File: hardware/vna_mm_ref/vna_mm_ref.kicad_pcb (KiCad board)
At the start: 4 copper layers, 213 parts, among them J201 Conn_Coaxial, J202 Conn_Coaxial, J401 Conn_Coaxial, J402 Conn_Coaxial, J501 Conn_02x10_Counter_Clockwise, K401 1-1462051-1, Q501 FDS6890A, SW501 SW_DIP_x02, SW502 SW_DIP_x02, U201 LTC6957xDD-3, U301 HMC1031, U401 DOCAT050F-010.0M, U402 74AHC1G04, U403 DRV8837C, U404 LTC6957xDD-3, U501 LTC4365DDB, U502 ADP7156, U503 ADP7156, U504 74AHC244, U505 LMT84DCK, X301 ABLNO-V-100.000MHZ

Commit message: layout of 100 MHz reference board
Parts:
- added H509: M.2, MountingHole:MountingHole_2.2mm_M2_Pad_Via, F.Cu at (161.2, 68.0)
- added H510: M.2, MountingHole:MountingHole_2.2mm_M2_Pad_Via, F.Cu at (158.2, 102.0)
- added H512: M.2, MountingHole:MountingHole_2.2mm_M2_Pad_Via, F.Cu at (208.0, 67.5)
- added H513: M.2, MountingHole:MountingHole_2.2mm_M2_Pad_Via, F.Cu at (251.5, 42.0)
- added H514: M.2, MountingHole:MountingHole_2.2mm_M2_Pad_Via, F.Cu at (196.0, 102.0)
- added H515: M.2, MountingHole:MountingHole_2.2mm_M2_Pad_Via, F.Cu at (141.5, 42.0)
- added H516: M.2, MountingHole:MountingHole_2.2mm_M2_Pad_Via, F.Cu at (186.0, 68.0)
- added J502: Conn_01x07, Connector_PinHeader_2.54mm:PinHeader_1x07_P2.54mm_Vertical, F.Cu at (188.0, 45.7)
- added R537: 10k, Resistor_SMD:R_0402_1005Metric, F.Cu at (213.8, 61.5)
- added TP504: TestPoint, vna_mm:TURRET_MILLMAX_2101, F.Cu at (141.5, 50.5)
- J501: value Conn_02x10_Counter_Clockwise -> Conn_02x10_Odd_Even; footprint Connector_PinHeader_2.54mm:PinHeader_2x11_P2.54mm_Vertical -> Connector_PinHeader_2.54mm:PinHeader_2x10_P2.54mm_Vertical
- TP503: value FAULT -> TestPoint; footprint TestPoint:TestPoint_Keystone_5015_Micro-Minature -> vna_mm:TURRET_MILLMAX_2101
- moved R515 246.7 mm to (250.5, 59.5)
- moved SW501 236.6 mm to (245.0, 58.5), turned to 180 degrees
- moved R520 227.1 mm to (239.5, 56.0), turned to 270 degrees
- moved R524 224.1 mm to (239.5, 59.0), turned to 270 degrees
- moved J501 192.1 mm to (210.8, 40.6), turned to 270 degrees
- moved R516 177.0 mm to (179.5, 57.5)
- moved C525 176.8 mm to (231.5, 60.2), turned to 0 degrees
- moved SW502 176.2 mm to (186.0, 59.0)
- moved R527 176.2 mm to (229.0, 59.2)
- moved C523 175.3 mm to (234.5, 59.7), turned to 270 degrees
- moved U505 173.3 mm to (232.0, 58.2)
- moved R521 172.3 mm to (185.5, 54.0)
- moved R525 172.3 mm to (188.0, 54.0)
- moved R509 167.8 mm to (217.5, 47.5), turned to 270 degrees
- moved D501 165.4 mm to (217.5, 50.7), turned to 270 degrees
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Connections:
- C527 pad 1: /PLL_EN -> /power_conn/INT_REF_EN
- J501 pad 10: GND -> /power_conn/SD_PLLCLK_EXT
- J501 pad 11: /power_conn/REF_SEL_EXT -> GND
- J501 pad 12: /power_conn/INT_REF_EN_EXT -> /power_conn/SD_REFOUT_EXT
- J501 pad 13: /power_conn/SD2_OUTPUT_EXT -> GND
- J501 pad 15: /power_conn/SD_REFOUT_EXT -> GND
- J501 pad 16: /power_conn/SD_PLLCLK_EXT -> /power_conn/SD2_OUTPUT_EXT
- J501 pad 17: /power_conn/RELAY_EN_EXT -> /power_conn/TEMP_SENSE
- J501 pad 18: (no net) -> /power_conn/INT_REF_EN_EXT
- J501 pad 2: VPP -> GND
- J501 pad 20: GND -> /power_conn/REF_SEL_EXT
- J501 pad 4: VPP -> GND
- J501 pad 6: GND -> /power_conn/LKD_EXT
- J501 pad 8: GND -> /power_conn/RELAY_EN_EXT
- J501 pad 9: /power_conn/TEMP_SENSE -> GND
- R302 pad 1: /PLL_EN -> +3V3
- R303 pad 2: /PLL_EN -> +3V3
- R501 pad 2: (no net) -> /power_conn/INT_REF_EN
- R534 pad 1: /PLL_EN -> /power_conn/INT_REF_EN
- TP503 pad 1: Net-(D504-Pad1) -> GND
- U201 pad 10: Net-(R206-Pad1) -> Net-(R207-Pad1)
- U201 pad 9: Net-(R207-Pad1) -> Net-(R206-Pad1)
- U504 pad 15: /power_conn/SD_REFOUT_EXT -> /power_conn/INT_REF_EN_EXT
- U504 pad 17: /power_conn/SD_PLLCLK_EXT -> /power_conn/REF_SEL_EXT
- U504 pad 6: /power_conn/REF_SEL_EXT -> /power_conn/SD_PLLCLK_EXT
- U504 pad 8: /power_conn/INT_REF_EN_EXT -> /power_conn/SD_REFOUT_EXT
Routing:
- net GND: track 0.00 -> 83.1 mm, vias 0 -> 107
- net Net-(C309-Pad1): track 0.00 -> 24.3 mm
- net Net-(K401-Pad11): track 0.00 -> 22.1 mm
- net Net-(C424-Pad2): track 0.00 -> 15.5 mm
- net Net-(K401-Pad1): track 0.00 -> 14.7 mm
- net +4V: track 0.00 -> 12.3 mm
- net Net-(C307-Pad2): track 0.00 -> 11.4 mm
- net Net-(C303-Pad1): track 0.00 -> 10.5 mm
- net Net-(C410-Pad1): track 0.00 -> 10.3 mm
- net Net-(C401-Pad2): track 0.00 -> 9.29 mm
- net Net-(C402-Pad2): track 0.00 -> 8.94 mm
- net Net-(C213-Pad2): track 0.00 -> 8.55 mm
- net Net-(K401-Pad14): track 0.00 -> 8.28 mm
- net Net-(C207-Pad1): track 0.00 -> 8.11 mm
- net Net-(C306-Pad1): track 0.00 -> 8.08 mm
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- added copper zone on F.Cu, net GND
- added copper zone on In1.Cu, net GND
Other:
- board outline added: 115.5 x 66 mm
- net class Default: clearance 0.2 -> 0.15; via_dia 0.8 -> 0.55; via_drill 0.4 -> 0.3
- rule trace_clearance: 0.2 -> 0.15
- rule trace_min: 0.2 -> 0.14
- rule via_min_drill: 0.3 -> 0.2
- rule via_min_size: 0.4 -> 0.45
- board text added: "4V"
- board text added: "EXT_CLK"
- board text added: "GND"
- board text added: "LKD"
- board text added: "REFOUT"
- board text added: "REF_EN"
- board text added: "REF_SEL"
- board text added: "RLY_EN"
- board text added: "SD1_OUT"
- board text added: "SD2_OUT"
- board text added: "TODO: VERIFY RELAY FOOTPRINT"
- board text added: "low phase noise 100 MHz reference 2019.11"

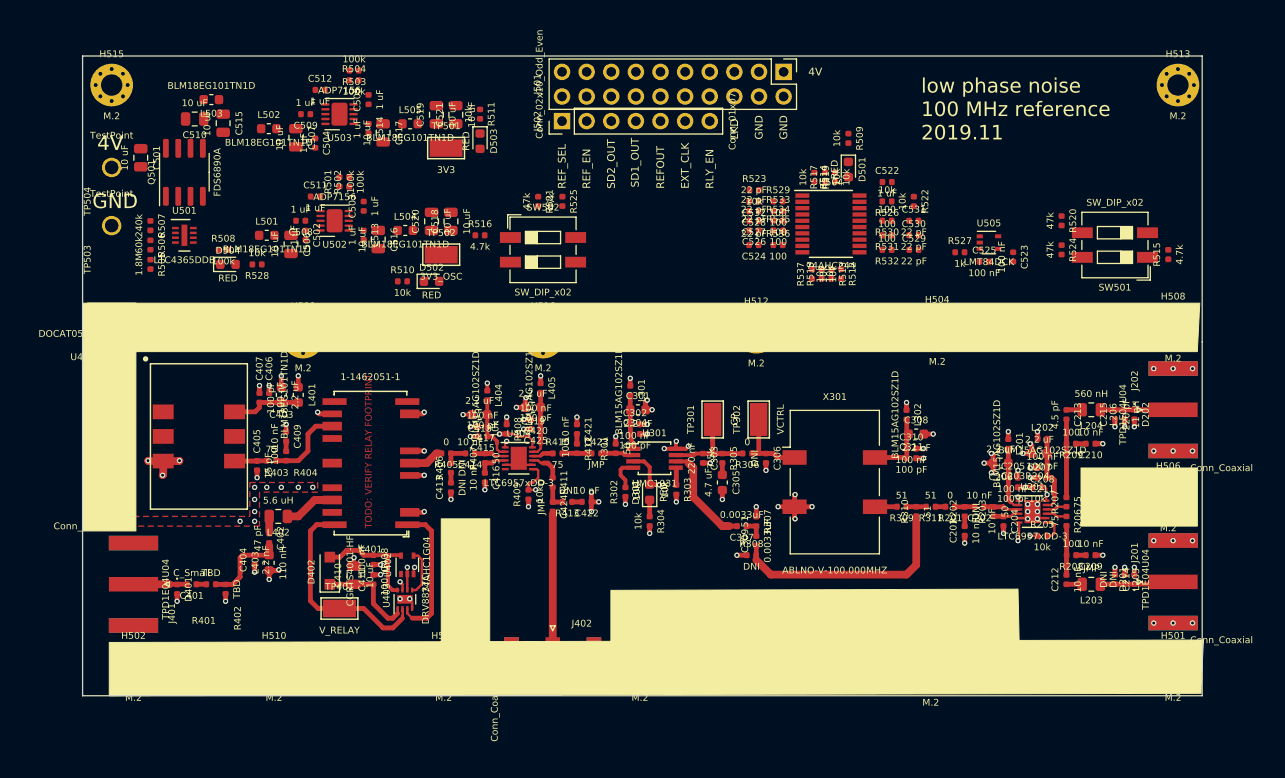
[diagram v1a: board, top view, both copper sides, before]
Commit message: work on layout of vna mm ref board
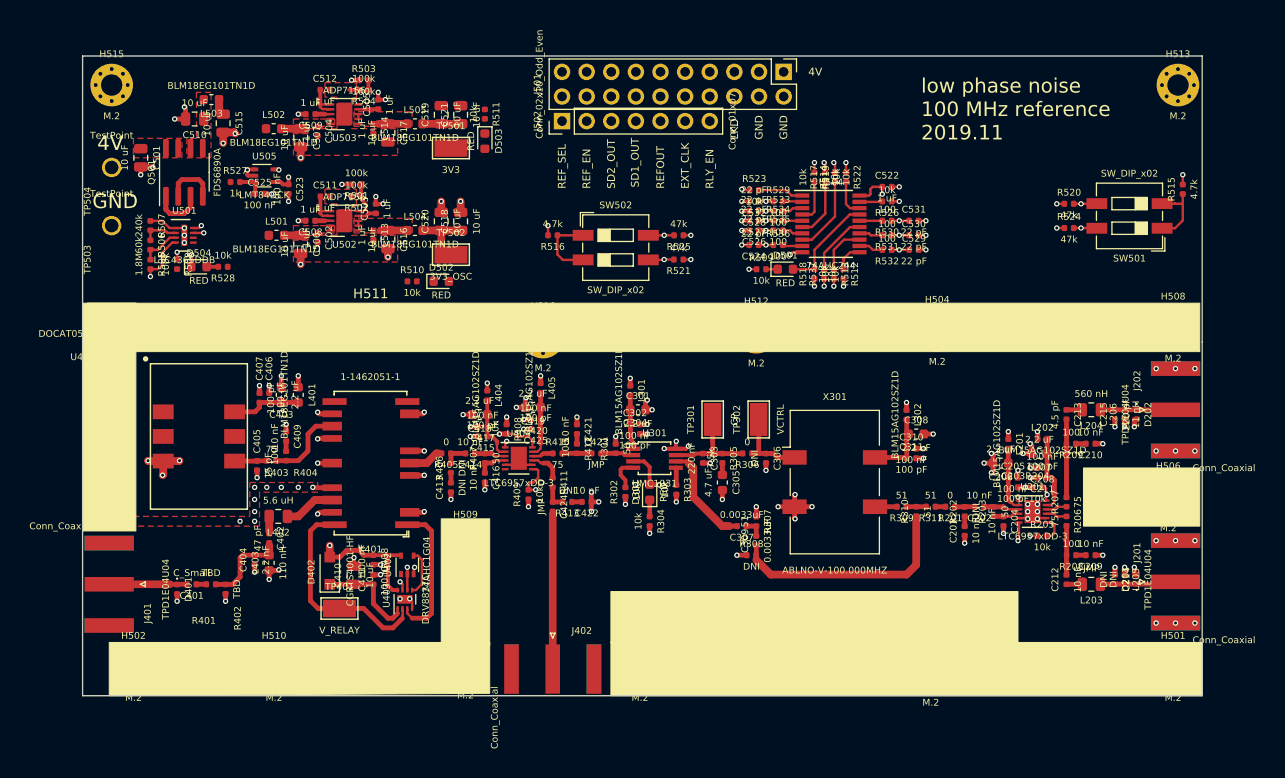
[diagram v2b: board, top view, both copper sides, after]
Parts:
- added H511: M.2, MountingHole:MountingHole_2.2mm_M2_Pad_Via, F.Cu at (168.2, 66.7)
- moved R527 75.1 mm to (154.2, 52.0)
- moved C523 75.1 mm to (159.8, 52.7)
- moved C525 75.1 mm to (156.8, 53.2)
- moved U505 75.1 mm to (157.2, 51.4)
- moved H509 27.3 mm to (178.0, 89.5)
- moved R509 16.2 mm to (208.5, 61.0), turned to 0 degrees
- moved R521 15.7 mm to (200.0, 60.0), turned to 180 degrees
- moved R525 12.5 mm to (200.0, 57.5), turned to 180 degrees
- moved D501 12.2 mm to (211.0, 61.0), turned to 0 degrees
- moved SW502 7.50 mm to (193.5, 58.8)
- moved R516 7.50 mm to (187.0, 57.5), turned to 180 degrees
- moved R522 7.43 mm to (217.2, 51.5)
- moved R515 6.90 mm to (252.0, 52.8)
- moved R508 5.00 mm to (148.2, 60.5), turned to 270 degrees
- moved R528 3.52 mm to (153.0, 60.8)
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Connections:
- K401 pad 15: (no net) -> GND
- K401 pad 17: (no net) -> GND
- K401 pad 19: (no net) -> GND
- K401 pad 21: (no net) -> GND
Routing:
- net GND: track 83.1 -> 133.8 mm, vias 107 -> 155
- net +3V3: track 6.19 -> 19.6 mm, vias 8 -> 15
- net /power_conn/REF_SEL_EXT: track 0.00 -> 10.7 mm
- net /power_conn/SD_REFOUT_EXT: track 0.00 -> 7.93 mm
- net Net-(R516-Pad1): track 0.00 -> 7.51 mm
- net Net-(R515-Pad1): track 0.00 -> 7.34 mm
- net +3.3VP: track 1.17 -> 8.45 mm
- net +4V: track 12.3 -> 18.9 mm, vias 0 -> 3
- net /power_conn/INT_REF_EN_EXT: track 0.00 -> 6.45 mm
- net /power_conn/SD_PLLCLK_EXT: track 0.00 -> 6.22 mm
- net Net-(Q501-Pad1): track 0.11 -> 5.84 mm
- net Net-(C511-Pad1): track 0.00 -> 5.70 mm
- net Net-(C512-Pad1): track 0.00 -> 5.68 mm
- net Net-(Q501-Pad2): track 0.00 -> 5.53 mm
- net VPP: track 0.00 -> 5.21 mm, vias 0 -> 1
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- added copper zone on F.Cu, net Net-(C502-Pad1)
- added copper zone on F.Cu, net Net-(C504-Pad1)
- added copper zone on F.Cu, net Net-(C510-Pad1)
- added copper zone on F.Cu, net Net-(C513-Pad1)
- added copper zone on F.Cu, net Net-(C514-Pad1)
- added copper zone on F.Cu, net VPP
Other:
- board text removed: "TODO: VERIFY RELAY FOOTPRINT"

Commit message: finished first pass layout of ref board
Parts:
- added H517: M.2, MountingHole:MountingHole_2.2mm_M2_Pad_Via, F.Cu at (213.8, 102.0)
- added H518: M.2, MountingHole:MountingHole_2.2mm_M2_Pad_Via, F.Cu at (141.2, 67.0)
- moved H503 13.2 mm to (141.2, 85.0)
- moved R503 8.06 mm to (159.5, 42.5), turned to 90 degrees
- moved R504 6.50 mm to (161.0, 42.5), turned to 270 degrees
- moved H512 5.77 mm to (213.8, 67.0)
- moved H516 5.10 mm to (191.0, 67.0)
- moved H507 3.78 mm to (229.8, 102.0)
- moved R515 3.61 mm to (250.0, 55.8)
- moved R520 3.61 mm to (238.3, 57.2)
- moved R524 3.61 mm to (238.3, 59.8)
- moved SW501 3.61 mm to (244.5, 58.5)
- moved R527 3.35 mm to (156.7, 54.2), turned to 180 degrees
- moved H504 3.10 mm to (229.8, 67.0)
- moved H502 2.50 mm to (141.2, 102.0)
- moved H511 1.99 mm to (166.2, 67.0)
- moved H510 1.75 mm to (160.0, 102.0)
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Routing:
- net /LKD: track 6.30 -> 128.9 mm, vias 2 -> 3
- net VPP: track 5.21 -> 115.3 mm, vias 1 -> 0
- net +3V3: track 19.6 -> 103.1 mm, vias 15 -> 27
- net /RELAY_EN: track 2.75 -> 86.1 mm
- net /REF_SEL: track 3.89 -> 74.2 mm, vias 2 -> 3
- net +4V: track 18.9 -> 88.1 mm, vias 3 -> 2
- net /SD_REFOUT: track 5.79 -> 74.1 mm
- net /SD2_OUTPUT: track 4.23 -> 69.0 mm, vias 1 -> 2
- net /SD1_OUTPUT: track 3.44 -> 65.0 mm, vias 2 -> 4
- net /SD_PLLCLK: track 6.20 -> 67.5 mm
- net /power_conn/INT_REF_EN: track 2.54 -> 52.3 mm
- net /power_conn/SD2_OUTPUT_EXT: track 3.02 -> 47.1 mm, vias 0 -> 1
- net /FILTA_REF: track 2.65 -> 46.6 mm, vias 1 -> 3
- net /power_conn/TEMP_SENSE: track 0.00 -> 43.3 mm, vias 0 -> 1
- net /power_conn/INT_REF_EN_EXT: track 6.45 -> 49.2 mm, vias 0 -> 1
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- added copper zone on B.Cu, net +3V3
- added copper zone on In2.Cu, net +3V3
- added copper zone on B.Cu, net GND
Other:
- outline, holes or cut-outs redrawn

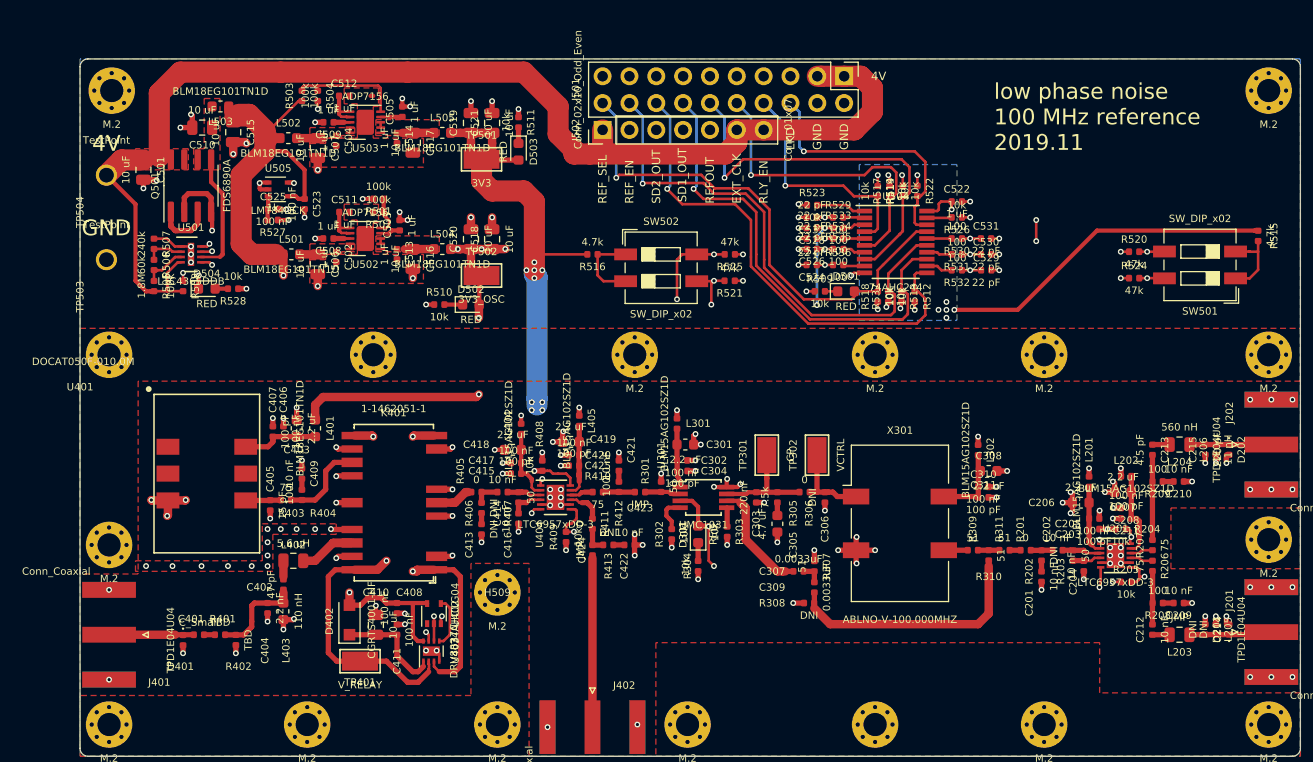
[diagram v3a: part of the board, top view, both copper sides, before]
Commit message: silkscreen cleanup
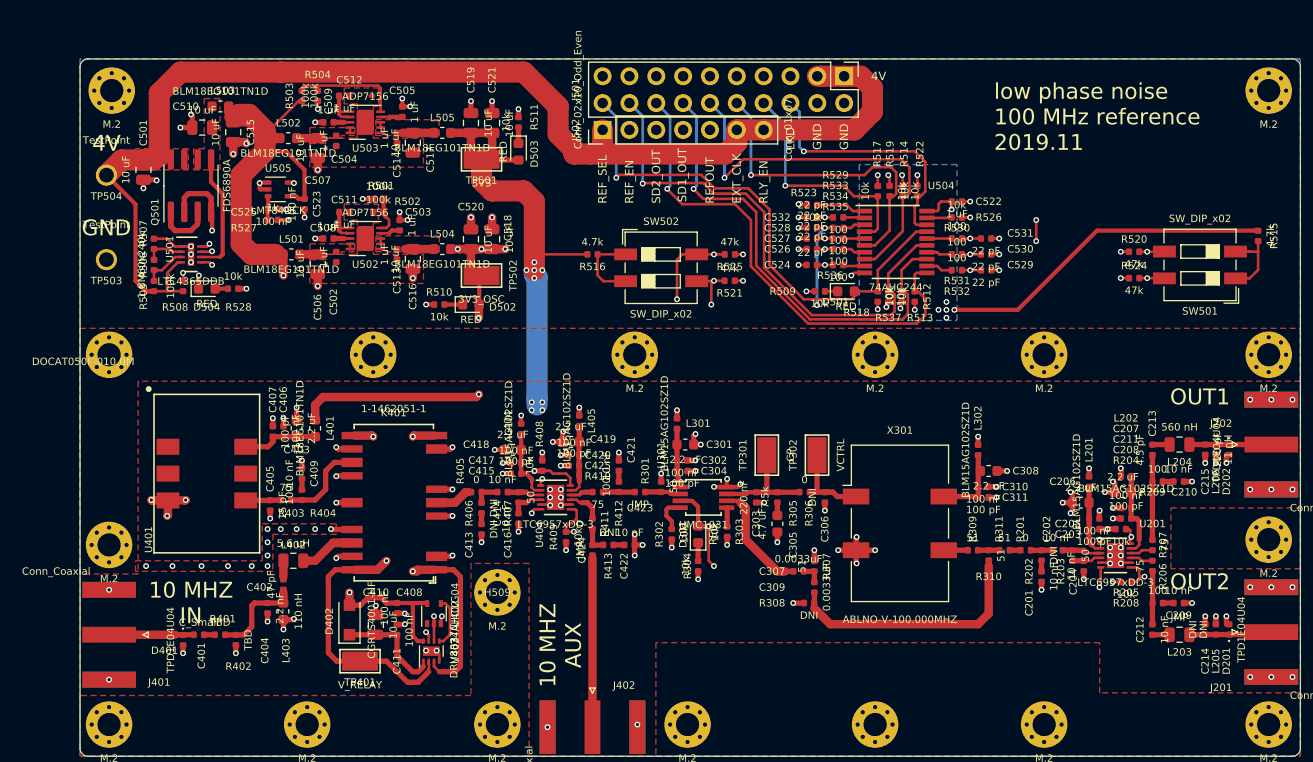
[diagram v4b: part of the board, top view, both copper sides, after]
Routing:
- net VPP: track 115.3 -> 117.0 mm
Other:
- board text added: "10 MHZ AUX"
- board text added: "10 MHZ IN"
- board text added: "OUT1"
- board text added: "OUT2"

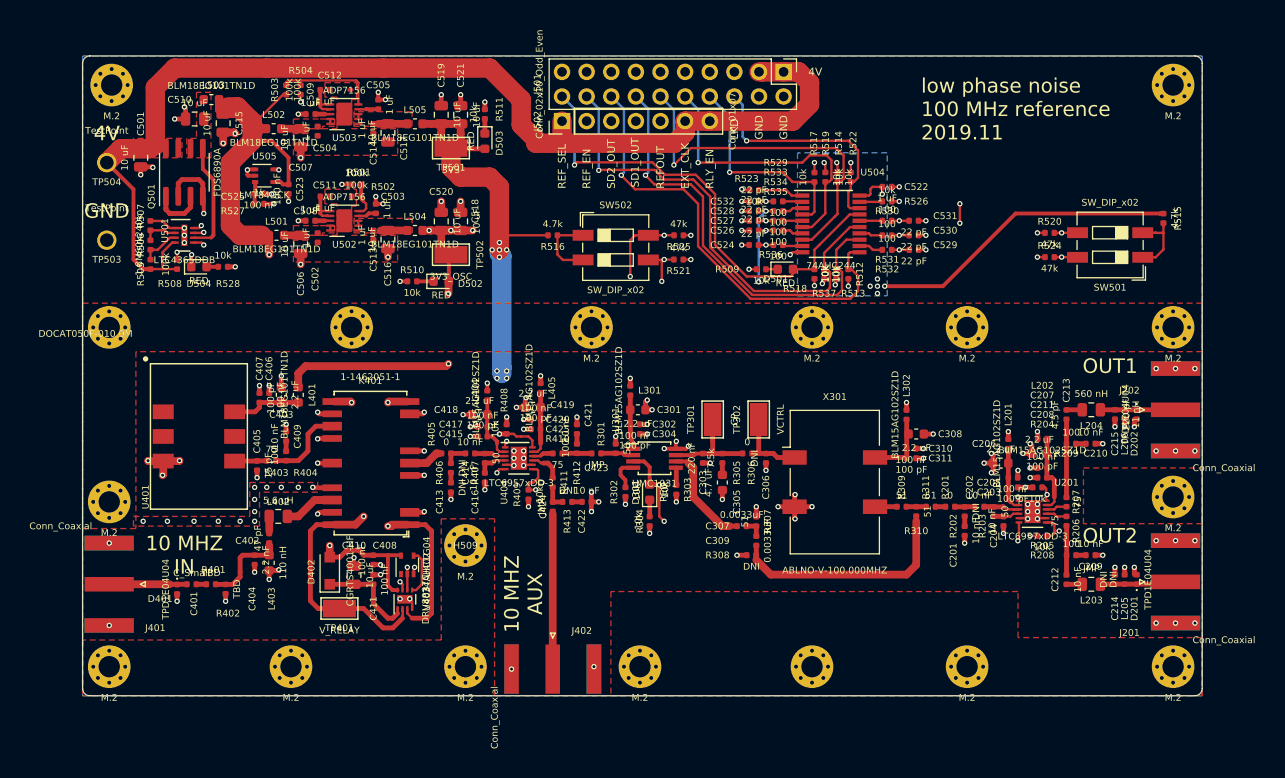
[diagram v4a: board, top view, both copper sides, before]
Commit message: added bulk decoupling caps to vna ref, silkscreen cleanup
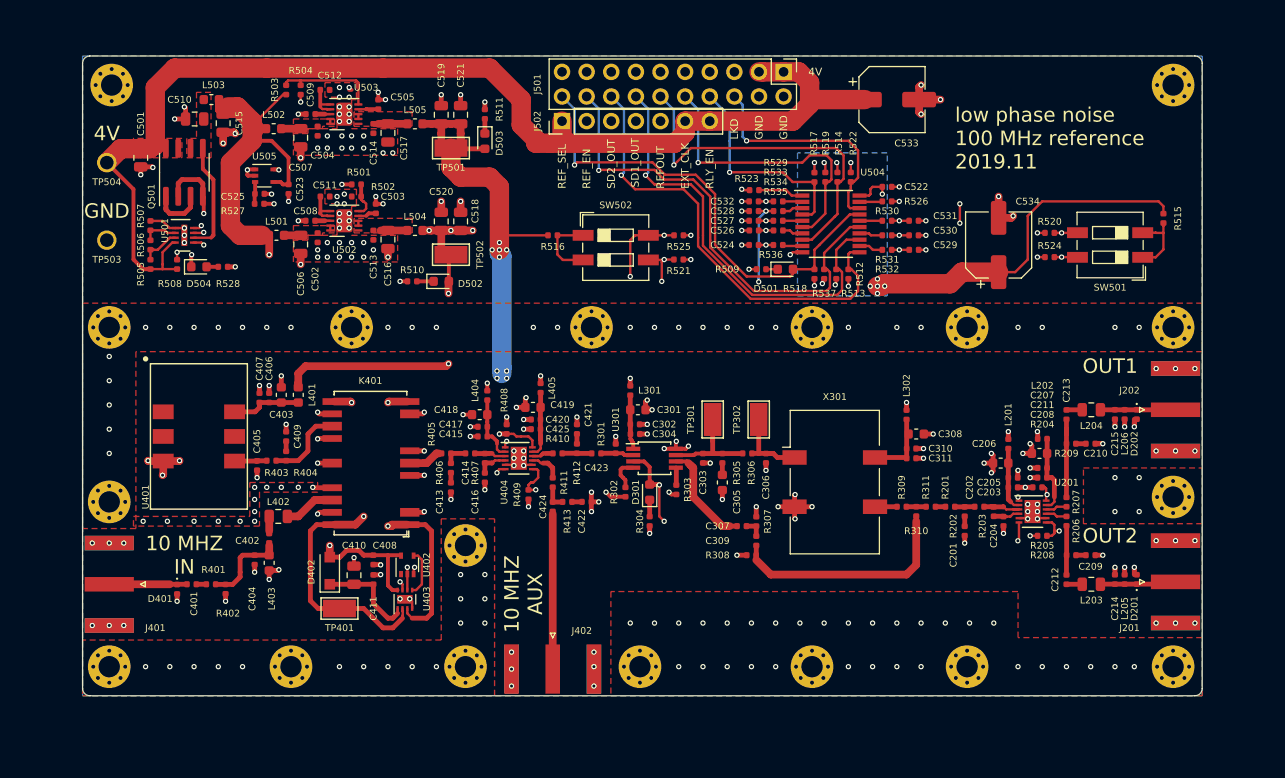
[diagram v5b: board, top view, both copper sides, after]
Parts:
- added C533: 330 uF, Capacitor_SMD:CP_Elec_6.3x5.9, F.Cu at (222.0, 43.5)
- added C534: 330 uF, Capacitor_SMD:CP_Elec_6.3x5.9, F.Cu at (233.0, 58.5)
- C401: value C_Small -> TBD
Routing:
- net GND: track 138.1 -> 147.3 mm, vias 175 -> 312
- net +3V3: track 103.1 -> 109.5 mm
- net VPP: track 117.0 -> 122.7 mm
- net /power_conn/INT_REF_EN: track 52.3 -> 54.8 mm
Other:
- rule pad_to_mask_clearance: 0.051 -> 0.021

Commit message: created BOM for vna mm ref
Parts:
- added G***: LOGO, vna_mm:cat, B.Cu at (215.0, 81.0)
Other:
- rule pad_to_mask_clearance: 0.021 -> 0.015
- rule solder_mask_min_width: 0.25 -> 0.15
- board text added: "JLCJLCJLCJLC"
